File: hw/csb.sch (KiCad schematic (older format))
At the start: 2 parts, among them J101 AMPSEAL_23_POS_VERT_BLUE_SEAL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, J102 AMPSEAL_8_POS_VERT_BLACK_SEAL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

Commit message: starting to draw version 4.0.0
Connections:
- net BEACON_2A is gone; now on net WORK_15A: J101.P$17 (S)
- net WORK_15A: now reaches J101.P$10 (S)
- net BACK_2A renamed BACK_4A
- net DRIVE_5A renamed DRIVE_15A
- net IN_2A renamed IN_4A
- net WIPER_2A renamed WIPER_4A
- net WORK_5A: no longer names the net of J101.P$11 (S)
- net WORK_5A: no longer J101.P$18 (S)
- new net BEACON_4A: J101.P$18 (S)
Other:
- moved on the sheet: J101J, J101K, J101Q, J101R
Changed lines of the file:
@@
 $EndComp
 Text Label 9400 3300 2    60   ~ 0
-DRIVE_5A
+DRIVE_15A
 Text Label 9400 3500 2    60   ~ 0
-WORK_5A
+WORK_15A
 $Sheet
 S 7900 4300 800  1100
@@
 $EndComp
 Text Label 9400 3200 2    60   ~ 0
-BEACON_2A
+BEACON_4A
 Text Label 9400 3400 2    60   ~ 0
-BACK_2A
+BACK_4A
 Text Label 9450 4750 2    60   ~ 0
-IN_2A
+IN_4A
 Text Label 9450 4650 2    60   ~ 0
-WIPER_2A
+WIPER_4A
 Text Label 9450 4850 2    60   ~ 0
 COOLER_30A
@@
 L AMPSEAL_23_POS_VERT_BLUE_SEALED_1-776228-5 J101
 U 10 1 595D41E8
-P 750 5250
-F 0 "J101" H 719 5333 45  0000 C CNN
-F 1 "AMPSEAL_23_POS_VERT_BLUE_SEALED_1-776228-5" H 750 5250 45  0001 L BNN
-F 2 "usevolt:AMPSEAL_23_POS_776200-1" H 780 5400 20  0001 C CNN
-F 3 "http://www.mouser.com/ds/2/418/NG_CD_776228_C13-683129.pdf" H 850 5220 60  0001 C CNN
-F 4 "571-1-776228-5" H 1250 5620 60  0001 C CNN "1st Source Part Number"
-F 5 "1-776228-5" H 1050 5420 60  0001 C CNN "Manufacturer Part Number"
-F 6 "Mouser" H 1150 5520 60  0001 C CNN "1st Source"
-F 7 "TE Connectivity" H 950 5320 60  0001 C CNN "Manufacturer"
-	10   750  5250
-	-1   0    0    -1
-$EndComp
-$Comp
-L AMPSEAL_23_POS_VERT_BLUE_SEALED_1-776228-5 J101
-U 11 1 595D4382
 P 9650 3600
-F 0 "J101" H 9618 3683 45  0000 C CNN
+F 0 "J101" H 9619 3683 45  0000 C CNN
 F 1 "AMPSEAL_23_POS_VERT_BLUE_SEALED_1-776228-5" H 9650 3600 45  0001 L BNN
 F 2 "usevolt:AMPSEAL_23_POS_776200-1" H 9680 3750 20  0001 C CNN
@@
 F 6 "Mouser" H 10050 3870 60  0001 C CNN "1st Source"
 F 7 "TE Connectivity" H 9850 3670 60  0001 C CNN "Manufacturer"
-	11   9650 3600
-	1    0    0    -1
+	10   9650 3600
+	1    0    0    -1
+$EndComp
+$Comp
+L AMPSEAL_23_POS_VERT_BLUE_SEALED_1-776228-5 J101
+U 11 1 595D4382
+P 750 5150
+F 0 "J101" H 718 5233 45  0000 C CNN
+F 1 "AMPSEAL_23_POS_VERT_BLUE_SEALED_1-776228-5" H 750 5150 45  0001 L BNN
+F 2 "usevolt:AMPSEAL_23_POS_776200-1" H 780 5300 20  0001 C CNN
+F 3 "http://www.mouser.com/ds/2/418/NG_CD_776228_C13-683129.pdf" H 850 5120 60  0001 C CNN
+F 4 "571-1-776228-5" H 1250 5520 60  0001 C CNN "1st Source Part Number"
+F 5 "1-776228-5" H 1050 5320 60  0001 C CNN "Manufacturer Part Number"
+F 6 "Mouser" H 1150 5420 60  0001 C CNN "1st Source"
+F 7 "TE Connectivity" H 950 5220 60  0001 C CNN "Manufacturer"
+	11   750  5150
+	-1   0    0    -1
 $EndComp
 $Comp
@@
 L AMPSEAL_23_POS_VERT_BLUE_SEALED_1-776228-5 J101
 U 17 1 595D4D74
+P 9900 3500
+F 0 "J101" H 9868 3583 45  0000 C CNN
+F 1 "AMPSEAL_23_POS_VERT_BLUE_SEALED_1-776228-5" H 9900 3500 45  0001 L BNN
+F 2 "usevolt:AMPSEAL_23_POS_776200-1" H 9930 3650 20  0001 C CNN
+F 3 "http://www.mouser.com/ds/2/418/NG_CD_776228_C13-683129.pdf" H 10000 3470 60  0001 C CNN
+F 4 "571-1-776228-5" H 10400 3870 60  0001 C CNN "1st Source Part Number"
+F 5 "1-776228-5" H 10200 3670 60  0001 C CNN "Manufacturer Part Number"
+F 6 "Mouser" H 10300 3770 60  0001 C CNN "1st Source"
+F 7 "TE Connectivity" H 10100 3570 60  0001 C CNN "Manufacturer"
+	17   9900 3500
+	1    0    0    -1
+$EndComp
+$Comp
+L AMPSEAL_23_POS_VERT_BLUE_SEALED_1-776228-5 J101
+U 18 1 595D4F1C
 P 9900 3100
 F 0 "J101" H 9868 3183 45  0000 C CNN
@@
 F 6 "Mouser" H 10300 3370 60  0001 C CNN "1st Source"
 F 7 "TE Connectivity" H 10100 3170 60  0001 C CNN "Manufacturer"
-	17   9900 3100
-	1    0    0    -1
-$EndComp
-$Comp
-L AMPSEAL_23_POS_VERT_BLUE_SEALED_1-776228-5 J101
-U 18 1 595D4F1C
-P 9900 3500
-F 0 "J101" H 9868 3583 45  0000 C CNN
-F 1 "AMPSEAL_23_POS_VERT_BLUE_SEALED_1-776228-5" H 9900 3500 45  0001 L BNN
-F 2 "usevolt:AMPSEAL_23_POS_776200-1" H 9930 3650 20  0001 C CNN
-F 3 "http://www.mouser.com/ds/2/418/NG_CD_776228_C13-683129.pdf" H 10000 3470 60  0001 C CNN
-F 4 "571-1-776228-5" H 10400 3870 60  0001 C CNN "1st Source Part Number"
-F 5 "1-776228-5" H 10200 3670 60  0001 C CNN "Manufacturer Part Number"
-F 6 "Mouser" H 10300 3770 60  0001 C CNN "1st Source"
-F 7 "TE Connectivity" H 10100 3570 60  0001 C CNN "Manufacturer"
-	18   9900 3500
-	1    0    0    -1
-$EndComp
+	18   9900 3100
+	1    0    0    -1
+$EndComp

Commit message: 3.1.0 hw created, not yet ordered
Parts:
- J101: symbol AMPSEAL_23_POS_VERT_BLUE_SEALED_1-776228-5 -> AMPSEAL_23_POS_VERT_BLUE_SEALED_1-776228-5-RESCUE-csb
- J102: symbol AMPSEAL_8_POS_VERT_BLACK_SEALED_1-776276-1 -> AMPSEAL_8_POS_VERT_BLACK_SEALED_1-776276-1-RESCUE-csb
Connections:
- net DRIVE_15A: now also J101.P$1 (S), J101.P$2 (S)
- net WORK_15A: now also J101.P$11 (S), J101.P$3 (S)
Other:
- moved on the sheet: J101A, J101B, J101C, J101H, J101I, J101J, J101K, J101M, J101O, J101P, J101Q, J101R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

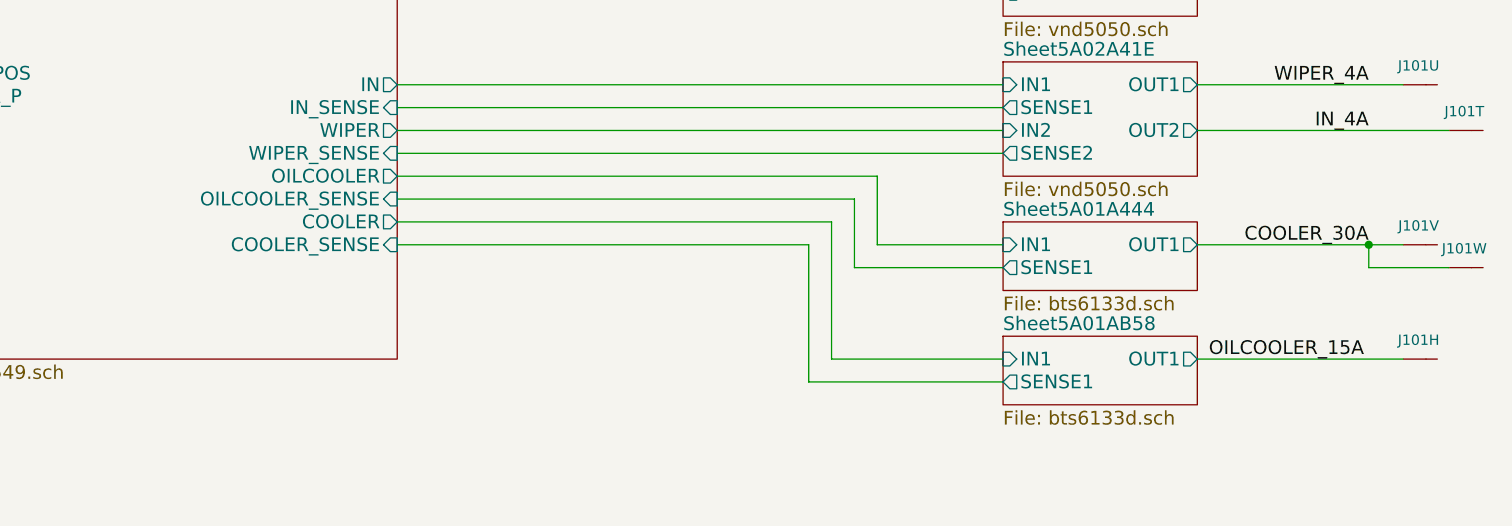
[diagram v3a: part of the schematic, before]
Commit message: oil cooler removed, 3.2.0 ready to order
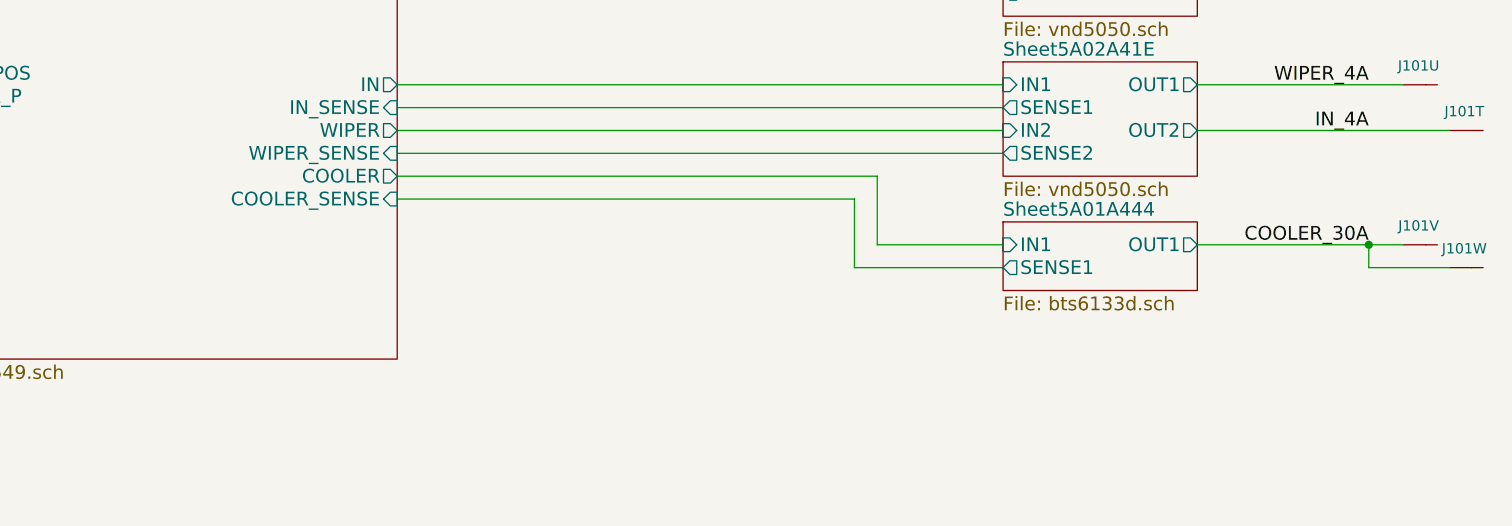
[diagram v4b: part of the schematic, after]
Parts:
- removed unit 8 of J101
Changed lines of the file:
@@
 $Descr A4 11693 8268
 encoding utf-8
-Sheet 1 9
+Sheet 1 8
 Title "Usewood Ceiling Supply Board"
 Date "2017-06-28"
@@
 $Comp
 L AMPSEAL_23_POS_VERT_BLUE_SEALED_1-776228-5-RESCUE-csb J101
-U 8 1 595D3EB6
-P 10900 5100
-F 0 "J101" H 10868 5183 45  0000 C CNN
-F 1 "AMPSEAL_23_POS_VERT_BLUE_SEALED_1-776228-5" H 10900 5100 45  0001 L BNN
-F 2 "usevolt:AMPSEAL_23_POS_776200-1" H 10930 5250 20  0001 C CNN
-F 3 "http://www.mouser.com/ds/2/418/NG_CD_776228_C13-683129.pdf" H 11000 5070 60  0001 C CNN
-F 4 "571-1-776228-5" H 11400 5470 60  0001 C CNN "1st Source Part Number"
-F 5 "1-776228-5" H 11200 5270 60  0001 C CNN "Manufacturer Part Number"
-F 6 "Mouser" H 11300 5370 60  0001 C CNN "1st Source"
-F 7 "TE Connectivity" H 11100 5170 60  0001 C CNN "Manufacturer"
-	8    10900 5100
-	1    0    0    -1
-$EndComp
-$Comp
-L AMPSEAL_23_POS_VERT_BLUE_SEALED_1-776228-5-RESCUE-csb J101
 U 9 1 595D404C
 P 10900 2100
@@
 F10 "BEACON" O R 6400 3100 60
 F11 "WIPER" O R 6400 4100 60
-F12 "COOLER" O R 6400 4500 60
+F12 "COOLER" O R 6400 4300 60
 F13 "WORK_SENSE" I R 6400 2800 60
 F14 "DRIVE_SENSE" I R 6400 2600 60
@@
 F17 "BACK_SENSE" I R 6400 3000 60
 F18 "WIPER_SENSE" I R 6400 4200 60
-F19 "COOLER_SENSE" I R 6400 4600 60
-F20 "OILCOOLER_SENSE" I R 6400 4400 60
-F21 "OILCOOLER" O R 6400 4300 60
+F19 "COOLER_SENSE" I R 6400 4400 60
 $EndSheet
-Text Label 9950 5100 0    60   ~ 0
-OILCOOLER_15A
 $Sheet
 S 9050 3100 850  500
@@
 F4 "SENSE1" O L 9050 4700 60
 $EndSheet
-$Sheet
-S 9050 5000 850  300
-U 5A01AB59
-F0 "Sheet5A01AB58" 60
-F1 "bts6133d.sch" 60
-F2 "OUT1" O R 9900 5100 60
-F3 "IN1" I L 9050 5100 60
-F4 "SENSE1" O L 9050 5200 60
-$EndSheet
 Wire Wire Line
 	3450 1150 3450 1300
@@
 Wire Wire Line
 	10750 3200 9900 3200
-Wire Wire Line
-	9900 5100 10800 5100
 Wire Wire Line
 	6400 2500 8350 2500
@@
 	8400 4400 6400 4400
 Wire Wire Line
-	6400 4500 8300 4500
-Wire Wire Line
-	8300 4500 8300 5100
-Wire Wire Line
-	8300 5100 9050 5100
-Wire Wire Line
-	9050 5200 8200 5200
-Wire Wire Line
-	8200 5200 8200 4600
-Wire Wire Line
-	8200 4600 6400 4600
-Wire Wire Line
 	6400 3100 8650 3100

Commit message: hw 3.3 created
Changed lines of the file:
@@
 U 5A01611C
 F0 "Sheet5A01611B" 60
-F1 "bts6133d.sch" 60
+F1 "vn5e010ah.sch" 60
 F2 "OUT1" O R 9900 2200 60
 F3 "IN1" I L 9050 2200 60
@@
 U 5A019746
 F0 "Sheet5A019745" 60
-F1 "bts6133d.sch" 60
+F1 "vn5e010ah.sch" 60
 F2 "OUT1" O R 9900 2700 60
 F3 "IN1" I L 9050 2700 60
@@
 U 5A01A445
 F0 "Sheet5A01A444" 60
-F1 "bts6133d.sch" 60
+F1 "vn5e010ah.sch" 60
 F2 "OUT1" O R 9900 4600 60
 F3 "IN1" I L 9050 4600 60
